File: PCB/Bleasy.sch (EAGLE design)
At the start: 14 parts, among them IC1 ATMEGA328-PU, Q1 8 MHz

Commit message: minor board changes, added Text
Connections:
- new net N$13: E1.UART_CTS, E1.UART_RTS
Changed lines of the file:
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@@
+</segment>
+</net>
+<net name="N$13" class="0">
+<segment>
+<pinref part="E1" gate="G$1" pin="UART_CTS"/>
+<pinref part="E1" gate="G$1" pin="UART_RTS"/>
+<wire x1="157.48" y1="127" x2="157.48" y2="124.46" width="0.1524" layer="91"/>
 </segment>
 </net>

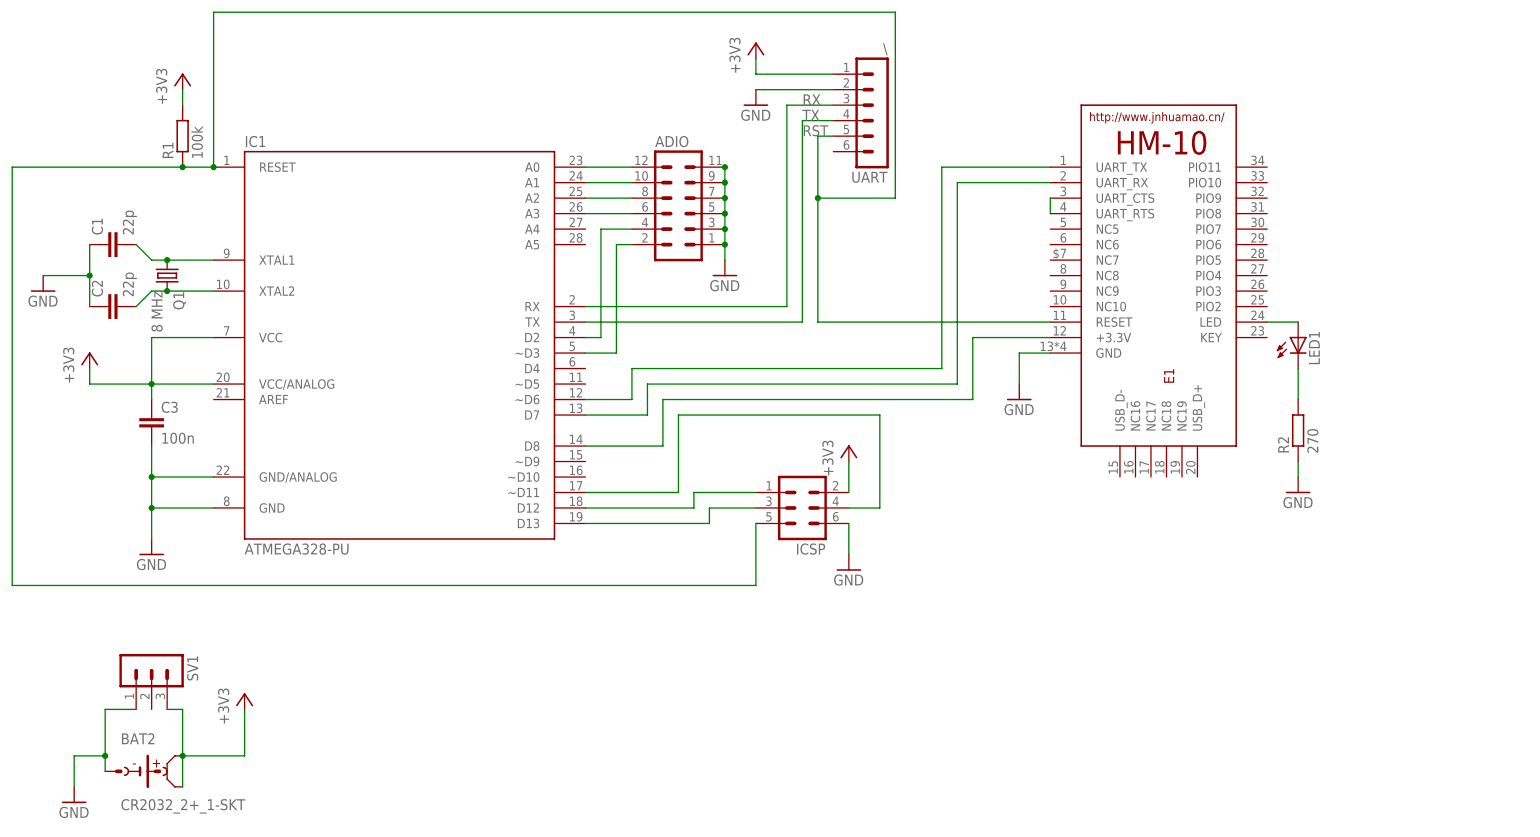
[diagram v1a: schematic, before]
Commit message: reordered Pingheaders, SMD
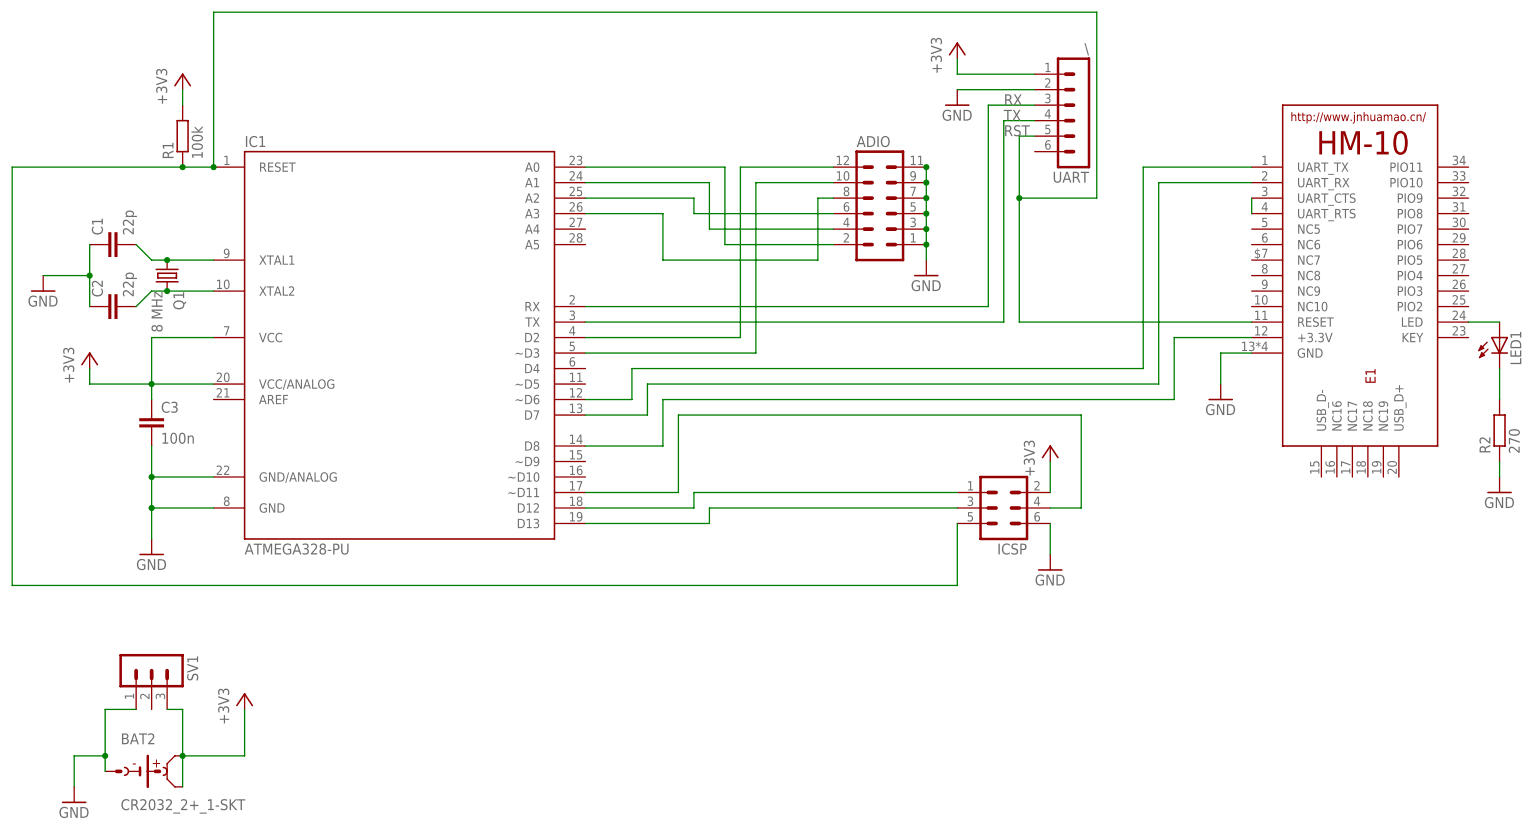
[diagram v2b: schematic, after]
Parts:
- R1, R2: device rcl:R-EU_0207/10 -> resistor:R-EU_R1206
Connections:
- net N$10: now also ADIO.4; no longer ADIO.10
- net N$11: now also ADIO.6; no longer ADIO.8
- net N$12: now also ADIO.8; no longer ADIO.6
- net N$4: now also ADIO.12, IC1.D2; no longer ADIO.2, IC1.~D3
- net N$5: now also ADIO.10, IC1.~D3; no longer ADIO.4, IC1.D2
- net N$9: now also ADIO.2; no longer ADIO.12
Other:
- moved on the sheet: ADIO, E1, ICSP, LED1, R2, UART

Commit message: added ground plane
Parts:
- renumbered SV1 to GND
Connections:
- net +3V3: now also UART.4; no longer UART.1
- net GND: now also UART.1; no longer UART.2
- net RX: now also UART.2; no longer UART.3
- net TX: now also UART.3; no longer UART.4
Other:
- moved on the sheet: UART
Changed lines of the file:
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@@
 <part name="GND7" library="supply1" deviceset="GND" device=""/>
 <part name="+3V5" library="supply1" deviceset="+3V3" device=""/>
-<part name="SV1" library="con-lstb" deviceset="MA03-1" device=""/>
+<part name="GND" library="con-lstb" deviceset="MA03-1" device=""/>
 <part name="ADIO" library="con-lstb" deviceset="MA06-2" device=""/>
 <part name="GND8" library="supply1" deviceset="GND" device=""/>
@@
 <instance part="R1" gate="G$1" x="15.24" y="137.16" rot="R90"/>
 <instance part="+3V2" gate="G$1" x="15.24" y="147.32"/>
-<instance part="UART" gate="1" x="162.56" y="139.7" rot="R180"/>
-<instance part="+3V3" gate="G$1" x="142.24" y="152.4"/>
+<instance part="UART" gate="1" x="165.1" y="139.7" rot="R180"/>
+<instance part="+3V3" gate="G$1" x="160.02" y="114.3"/>
 <instance part="GND3" gate="1" x="142.24" y="142.24"/>
 <instance part="IC1" gate="1" x="50.8" y="104.14"/>
@@
 <instance part="GND7" gate="1" x="-2.54" y="27.94"/>
 <instance part="+3V5" gate="G$1" x="25.4" y="45.72"/>
-<instance part="SV1" gate="G$1" x="10.16" y="50.8" rot="R270"/>
+<instance part="GND" gate="G$1" x="10.16" y="50.8" rot="R270"/>
 <instance part="ADIO" gate="1" x="129.54" y="127"/>
 <instance part="GND8" gate="1" x="137.16" y="114.3"/>
@@
 </segment>
 <segment>
-<pinref part="GND3" gate="1" pin="GND"/>
-<wire x1="142.24" y1="144.78" x2="154.94" y2="144.78" width="0.1524" layer="91"/>
-<pinref part="UART" gate="1" pin="2"/>
-</segment>
-<segment>
 <pinref part="GND7" gate="1" pin="GND"/>
 <wire x1="-2.54" y1="30.48" x2="-2.54" y2="35.56" width="0.1524" layer="91"/>
 <wire x1="-2.54" y1="35.56" x2="2.54" y2="35.56" width="0.1524" layer="91"/>
-<pinref part="SV1" gate="G$1" pin="1"/>
+<pinref part="GND" gate="G$1" pin="1"/>
 <wire x1="7.62" y1="43.18" x2="2.54" y2="43.18" width="0.1524" layer="91"/>
 <wire x1="2.54" y1="43.18" x2="2.54" y2="35.56" width="0.1524" layer="91"/>
@@
 <pinref part="R2" gate="G$1" pin="1"/>
 <wire x1="231.14" y1="83.82" x2="231.14" y2="81.28" width="0.1524" layer="91"/>
+</segment>
+<segment>
+<pinref part="GND3" gate="1" pin="GND"/>
+<wire x1="142.24" y1="144.78" x2="142.24" y2="147.32" width="0.1524" layer="91"/>
+<wire x1="142.24" y1="147.32" x2="157.48" y2="147.32" width="0.1524" layer="91"/>
+<pinref part="UART" gate="1" pin="1"/>
 </segment>
 </net>
@@
 </segment>
 <segment>
-<pinref part="+3V3" gate="G$1" pin="+3V3"/>
-<wire x1="142.24" y1="149.86" x2="142.24" y2="147.32" width="0.1524" layer="91"/>
-<pinref part="UART" gate="1" pin="1"/>
-<wire x1="142.24" y1="147.32" x2="154.94" y2="147.32" width="0.1524" layer="91"/>
-</segment>
-<segment>
 <pinref part="+3V5" gate="G$1" pin="+3V3"/>
 <wire x1="15.24" y1="35.56" x2="25.4" y2="35.56" width="0.1524" layer="91"/>
 <wire x1="25.4" y1="35.56" x2="25.4" y2="43.18" width="0.1524" layer="91"/>
-<pinref part="SV1" gate="G$1" pin="3"/>
+<pinref part="GND" gate="G$1" pin="3"/>
 <wire x1="12.7" y1="43.18" x2="15.24" y2="43.18" width="0.1524" layer="91"/>
 <wire x1="15.24" y1="43.18" x2="15.24" y2="35.56" width="0.1524" layer="91"/>
@@
 <pinref part="BAT2" gate="B1" pin="POS2"/>
 <wire x1="15.24" y1="30.48" x2="15.24" y2="35.56" width="0.1524" layer="91"/>
+</segment>
+<segment>
+<pinref part="+3V3" gate="G$1" pin="+3V3"/>
+<wire x1="160.02" y1="111.76" x2="152.4" y2="111.76" width="0.1524" layer="91"/>
+<wire x1="152.4" y1="111.76" x2="152.4" y2="139.7" width="0.1524" layer="91"/>
+<pinref part="UART" gate="1" pin="4"/>
+<wire x1="152.4" y1="139.7" x2="157.48" y2="139.7" width="0.1524" layer="91"/>
 </segment>
 </net>
@@
 <wire x1="-12.7" y1="132.08" x2="15.24" y2="132.08" width="0.1524" layer="91"/>
 <junction x="15.24" y="132.08"/>
-<pinref part="UART" gate="1" pin="5"/>
-<wire x1="154.94" y1="137.16" x2="152.4" y2="137.16" width="0.1524" layer="91"/>
-<wire x1="152.4" y1="106.68" x2="152.4" y2="127" width="0.1524" layer="91"/>
-<wire x1="152.4" y1="127" x2="152.4" y2="137.16" width="0.1524" layer="91"/>
-<wire x1="152.4" y1="127" x2="165.1" y2="127" width="0.1524" layer="91"/>
-<wire x1="165.1" y1="127" x2="165.1" y2="157.48" width="0.1524" layer="91"/>
-<wire x1="165.1" y1="157.48" x2="20.32" y2="157.48" width="0.1524" layer="91"/>
+<wire x1="170.18" y1="106.68" x2="170.18" y2="124.46" width="0.1524" layer="91"/>
+<wire x1="154.94" y1="124.46" x2="170.18" y2="124.46" width="0.1524" layer="91"/>
+<wire x1="170.18" y1="124.46" x2="170.18" y2="157.48" width="0.1524" layer="91"/>
+<wire x1="170.18" y1="157.48" x2="20.32" y2="157.48" width="0.1524" layer="91"/>
 <wire x1="20.32" y1="157.48" x2="20.32" y2="132.08" width="0.1524" layer="91"/>
-<junction x="152.4" y="127"/>
 <label x="149.86" y="137.16" size="1.778" layer="95"/>
 <pinref part="E1" gate="G$1" pin="RESET"/>
-<wire x1="152.4" y1="106.68" x2="190.5" y2="106.68" width="0.1524" layer="91"/>
+<wire x1="170.18" y1="106.68" x2="190.5" y2="106.68" width="0.1524" layer="91"/>
+<wire x1="154.94" y1="124.46" x2="154.94" y2="137.16" width="0.1524" layer="91"/>
+<pinref part="UART" gate="1" pin="5"/>
+<wire x1="154.94" y1="137.16" x2="157.48" y2="137.16" width="0.1524" layer="91"/>
 </segment>
 </net>
@@
 <segment>
 <wire x1="81.28" y1="109.22" x2="147.32" y2="109.22" width="0.1524" layer="91"/>
-<wire x1="147.32" y1="109.22" x2="147.32" y2="142.24" width="0.1524" layer="91"/>
-<pinref part="UART" gate="1" pin="3"/>
-<wire x1="147.32" y1="142.24" x2="154.94" y2="142.24" width="0.1524" layer="91"/>
+<wire x1="147.32" y1="109.22" x2="147.32" y2="144.78" width="0.1524" layer="91"/>
 <pinref part="IC1" gate="1" pin="RX"/>
 <label x="149.86" y="142.24" size="1.778" layer="95"/>
+<wire x1="147.32" y1="144.78" x2="157.48" y2="144.78" width="0.1524" layer="91"/>
+<pinref part="UART" gate="1" pin="2"/>
 </segment>
 </net>
@@
 <segment>
 <wire x1="81.28" y1="106.68" x2="149.86" y2="106.68" width="0.1524" layer="91"/>
-<wire x1="149.86" y1="106.68" x2="149.86" y2="139.7" width="0.1524" layer="91"/>
-<pinref part="UART" gate="1" pin="4"/>
-<wire x1="149.86" y1="139.7" x2="154.94" y2="139.7" width="0.1524" layer="91"/>
+<wire x1="149.86" y1="106.68" x2="149.86" y2="142.24" width="0.1524" layer="91"/>
 <pinref part="IC1" gate="1" pin="TX"/>
 <label x="149.86" y="139.7" size="1.778" layer="95"/>
-</segment>
-</net>
+<pinref part="UART" gate="1" pin="3"/>
+<wire x1="149.86" y1="142.24" x2="157.48" y2="142.24" width="0.1524" layer="91"/>
+</segment>
+</net>
